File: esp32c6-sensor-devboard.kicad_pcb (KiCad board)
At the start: 4 copper layers, 183 parts, among them J1 Conn_01x04_Pin, J2 Micro_SD_Card_Det1, J3 Screw_Terminal_01x02, J4 USB_C_Receptacle_USB2.0_14P, J5 Screw_Terminal_01x02, J6 Screw_Terminal_01x06, J7 Screw_Terminal_01x04, J8 Conn_01x04_Pin, J9 Conn_01x03_Pin, SW1 SW_Push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

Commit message: pcb: refine layout
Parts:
- moved TP1 170.6 mm to (188.0, 92.6), turned to 90 degrees
- moved TP4 169.2 mm to (188.0, 89.1), turned to 90 degrees
- moved C46 168.5 mm to (188.3, 80.8), turned to 90 degrees
- moved D8 168.3 mm to (184.3, 98.6), turned to -90 degrees
- moved R56 167.6 mm to (183.0, 78.8)
- moved R53 165.9 mm to (185.3, 90.2), turned to 90 degrees
- moved C45 165.9 mm to (184.5, 92.6), turned to 180 degrees
- moved TP7 164.3 mm to (186.0, 79.6), turned to 90 degrees
- moved R54 163.8 mm to (183.8, 90.2), turned to -90 degrees
- moved U13 163.8 mm to (185.3, 84.3), turned to 0 degrees
- moved C47 162.4 mm to (183.3, 88.1), turned to 180 degrees
- moved R55 159.4 mm to (183.0, 80.3), turned to 0 degrees
- moved TP2 158.7 mm to (179.8, 92.6), turned to 90 degrees
- moved TP5 157.2 mm to (179.8, 89.1), turned to 90 degrees
- moved D6 156.7 mm to (176.0, 98.6), turned to -90 degrees
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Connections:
- J7 pad 1: /I1 -> GND
- J7 pad 2: /I2 -> /I3
- J7 pad 3: /I3 -> /I2
- J7 pad 4: GND -> /I1
- R14 pad 2: unconnected-(R14-Pad2) -> /ESP_D-

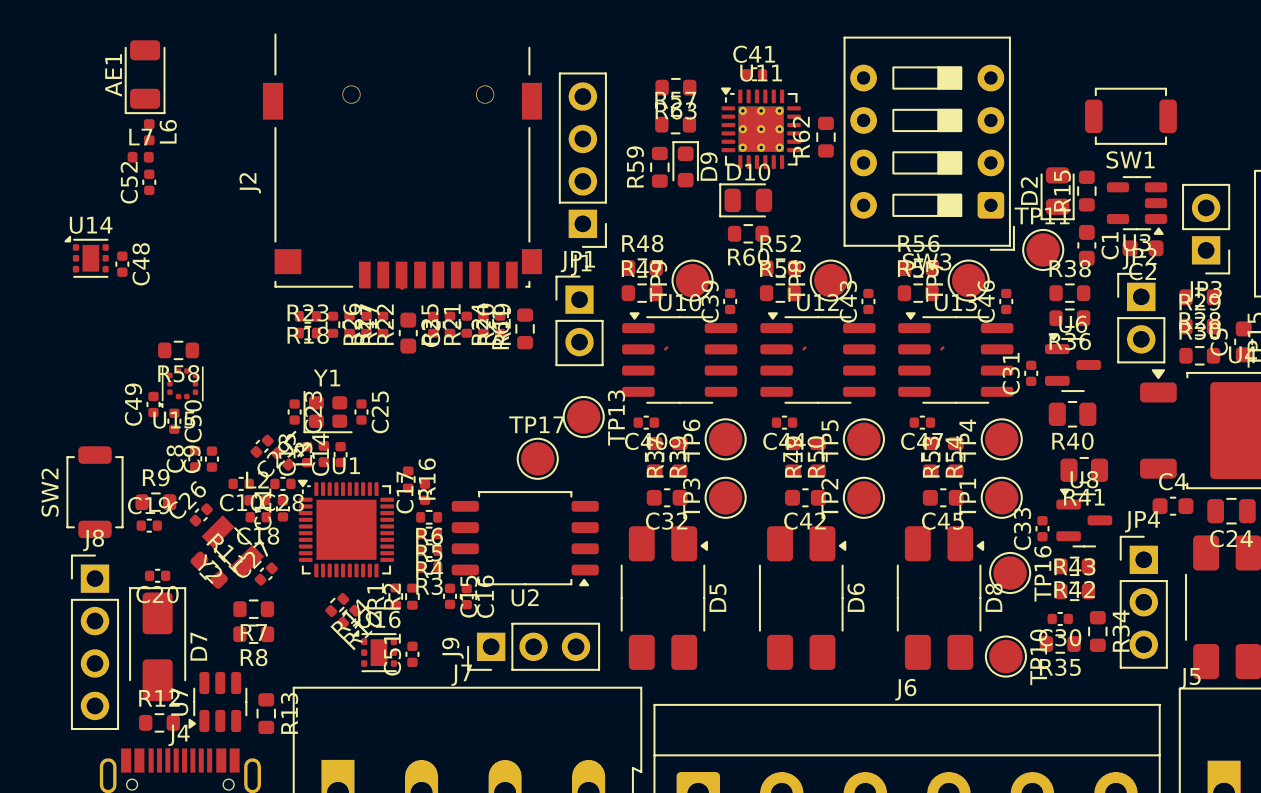
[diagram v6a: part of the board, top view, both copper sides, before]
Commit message: pcb: area reduction
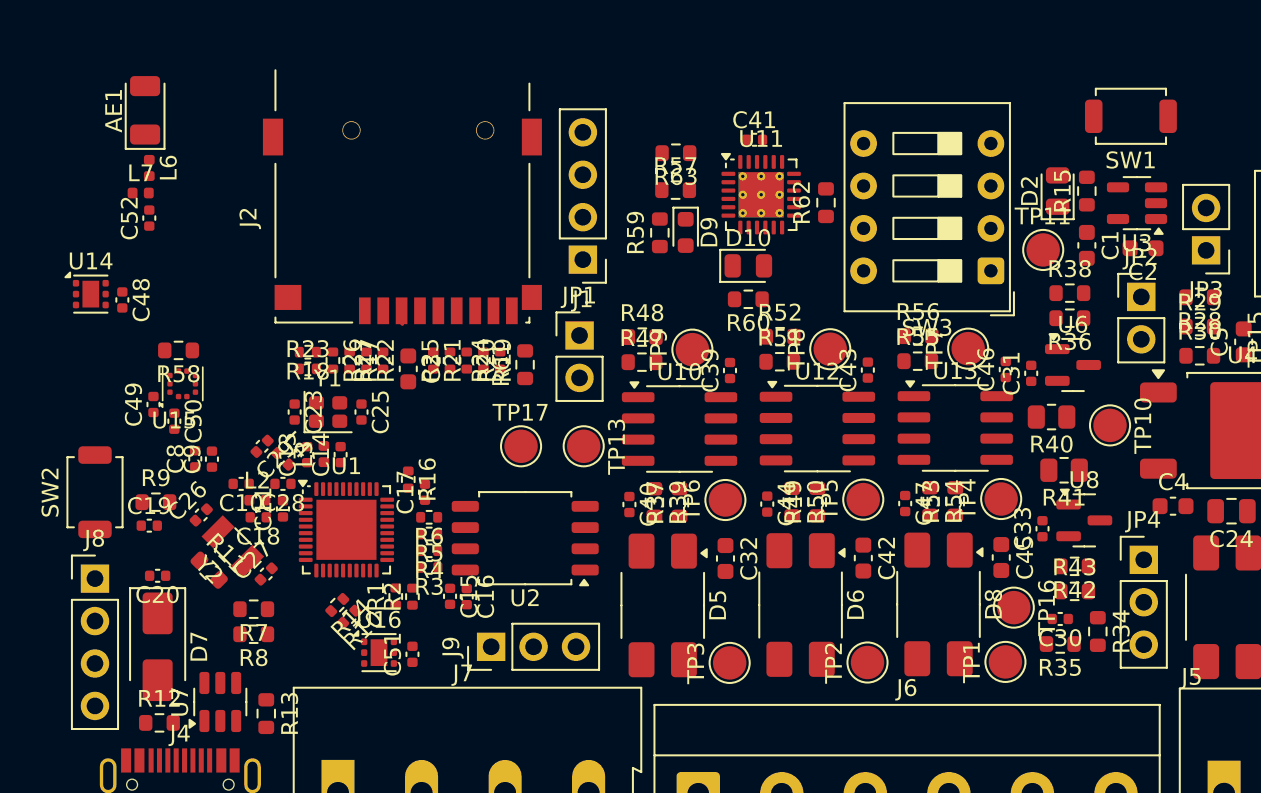
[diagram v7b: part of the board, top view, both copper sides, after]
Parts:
- moved TP10 15.2 mm to (194.5, 88.2)
- moved TP3 9.88 mm to (171.7, 102.5)
- moved TP2 9.86 mm to (180.0, 102.4)
- moved TP1 9.82 mm to (188.2, 102.4)
- moved C32 5.04 mm to (171.5, 96.2), turned to -90 degrees
- moved C40 5.00 mm to (165.7, 93.0), turned to -90 degrees
- moved C42 5.00 mm to (179.7, 96.2), turned to -90 degrees
- moved C44 4.98 mm to (174.0, 93.0), turned to -90 degrees
- moved C45 4.98 mm to (188.0, 96.2), turned to -90 degrees
- moved C47 4.95 mm to (182.2, 92.9), turned to -90 degrees
- moved C39 4.13 mm to (171.8, 85.0)
- moved R47 4.13 mm to (166.5, 84.5)
- moved R48 4.13 mm to (166.5, 83.0)
- moved TP9 4.13 mm to (169.5, 83.7)
- moved U10 4.13 mm to (168.7, 88.5)
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
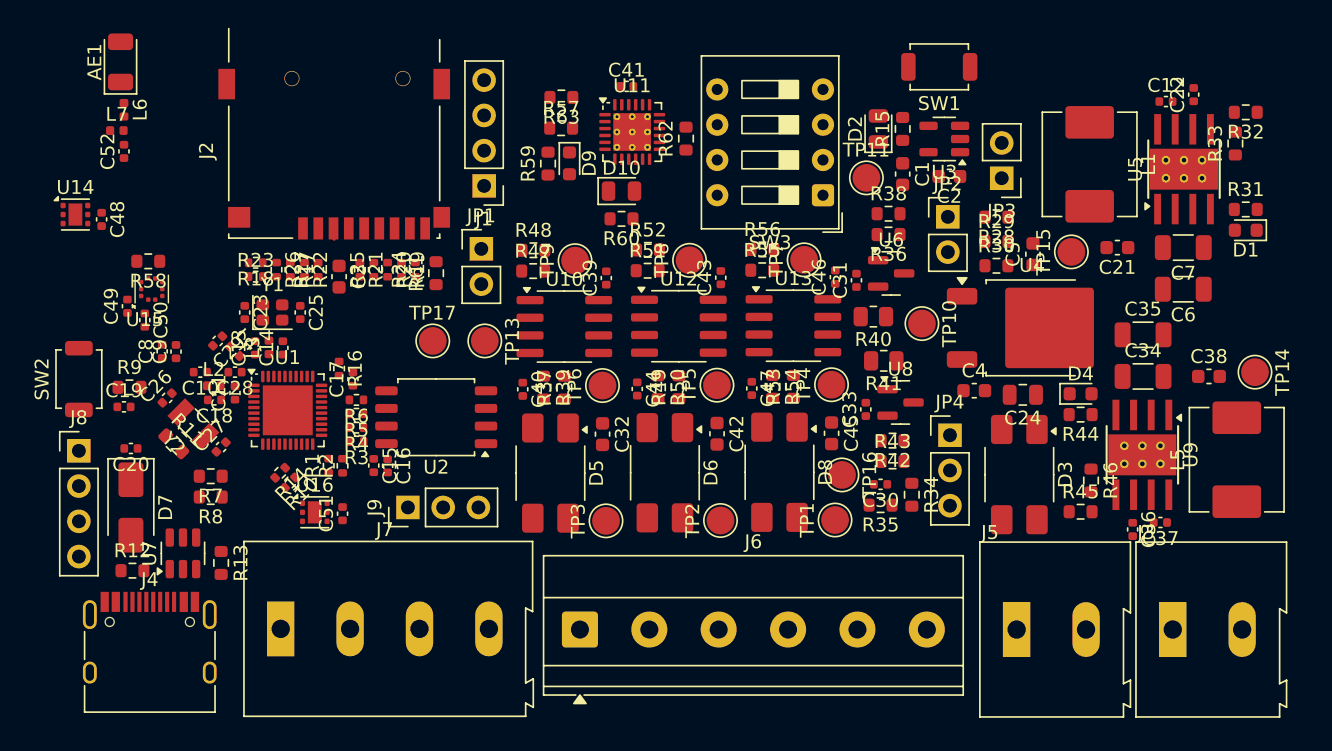
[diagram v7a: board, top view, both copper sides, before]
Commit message: pcb: add board outline
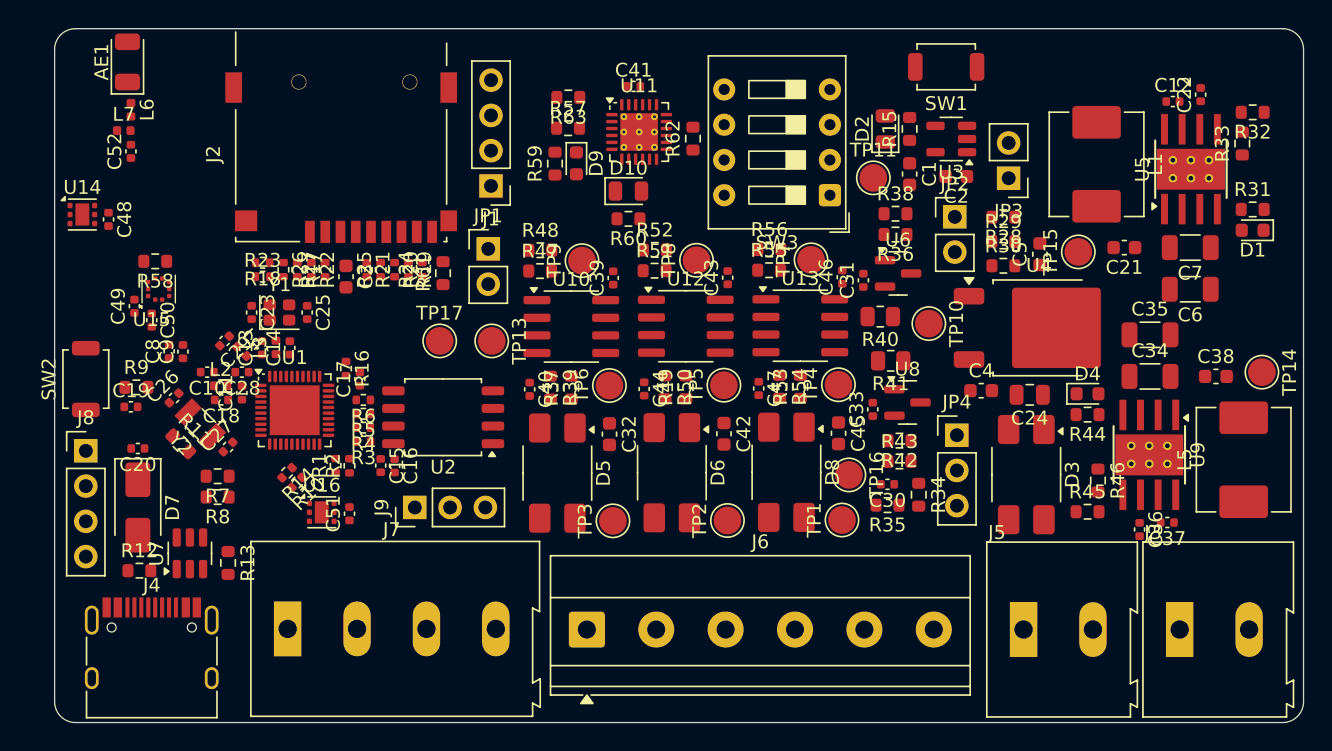
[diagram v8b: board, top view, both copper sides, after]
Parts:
- moved J2 0.56 mm to (152.7, 79.4)
- moved AE1 0.50 mm to (137.2, 69.4)
- moved C1 0.50 mm to (193.6, 77.5)
- moved C10 0.50 mm to (143.0, 91.8)
- moved C11 0.50 mm to (145.5, 93.2)
- moved C12 0.50 mm to (212.6, 72.2)
- moved C13 0.50 mm to (146.9, 90.0)
- moved C14 0.50 mm to (148.9, 90.0)
- moved C15 0.50 mm to (155.5, 98.5)
- moved C16 0.50 mm to (156.5, 98.5)
- moved C17 0.50 mm to (154.0, 92.2)
- moved C18 0.50 mm to (144.0, 93.8)
- moved C19 0.50 mm to (137.5, 94.2)
- moved C2 0.50 mm to (197.0, 77.7)
- moved C20 0.50 mm to (138.0, 97.2)
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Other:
- board outline added: 90 x 50 mm
